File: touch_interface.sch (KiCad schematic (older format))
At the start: 15 parts

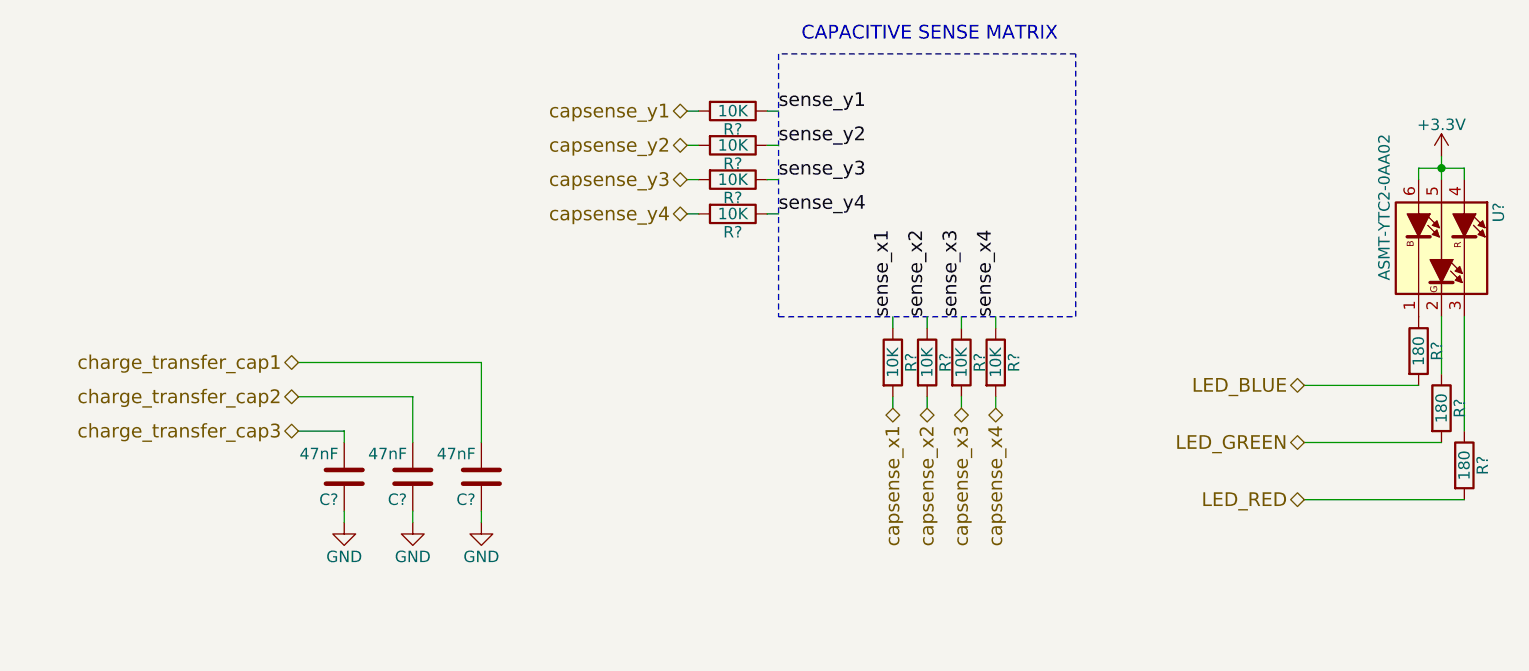
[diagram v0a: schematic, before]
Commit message: Make top-level connections between microcontroller and everything else
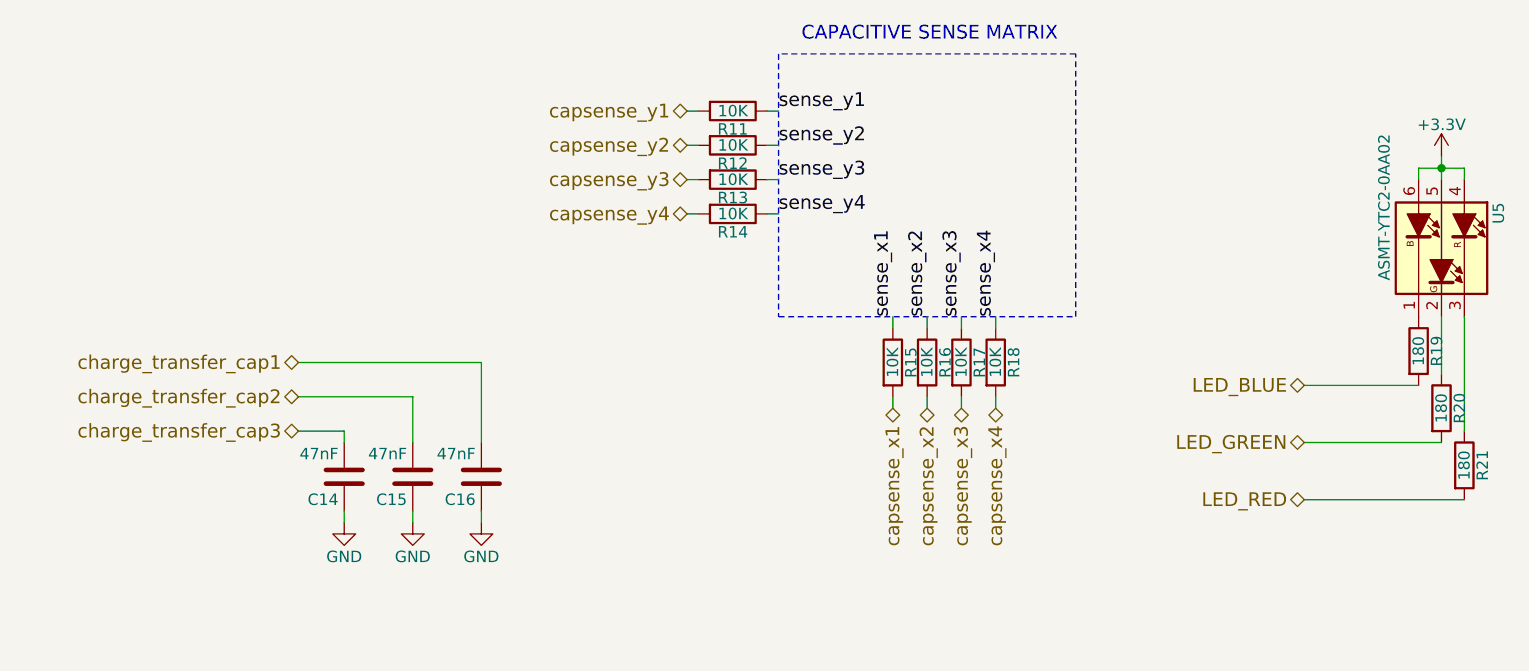
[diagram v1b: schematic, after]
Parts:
- gave numbers to parts that had none: 15
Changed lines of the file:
@@
 charge_transfer_cap3
 $Comp
-L C C?
+L C C14
 U 1 1 59A254BC
 P 2450 3950
-F 0 "C?" H 2475 4050 50  0000 L CNN
+F 0 "C14" H 2475 4050 50  0000 L CNN
 F 1 "47nF" H 2475 3850 50  0000 L CNN
 F 2 "" H 2488 3800 50  0001 C CNN
@@
 $EndComp
 $Comp
-L C C?
+L C C15
 U 1 1 59A25537
 P 2750 3950
-F 0 "C?" H 2775 4050 50  0000 L CNN
+F 0 "C15" H 2775 4050 50  0000 L CNN
 F 1 "47nF" H 2775 3850 50  0000 L CNN
 F 2 "" H 2788 3800 50  0001 C CNN
@@
 $EndComp
 $Comp
-L C C?
+L C C16
 U 1 1 59A25555
 P 3050 3950
-F 0 "C?" H 3075 4050 50  0000 L CNN
+F 0 "C16" H 3075 4050 50  0000 L CNN
 F 1 "47nF" H 3075 3850 50  0000 L CNN
 F 2 "" H 3088 3800 50  0001 C CNN
@@
 $EndComp
 $Comp
-L GND #PWR?
+L GND #PWR030
 U 1 1 59A25575
 P 2450 4150
-F 0 "#PWR?" H 2450 3900 50  0001 C CNN
+F 0 "#PWR030" H 2450 3900 50  0001 C CNN
 F 1 "GND" H 2450 4000 50  0000 C CNN
 F 2 "" H 2450 4150 50  0001 C CNN
@@
 	2450 4100 2450 4150
 $Comp
-L GND #PWR?
+L GND #PWR031
 U 1 1 59A255BB
 P 2750 4150
-F 0 "#PWR?" H 2750 3900 50  0001 C CNN
+F 0 "#PWR031" H 2750 3900 50  0001 C CNN
 F 1 "GND" H 2750 4000 50  0000 C CNN
 F 2 "" H 2750 4150 50  0001 C CNN
@@
 $EndComp
 $Comp
-L GND #PWR?
+L GND #PWR032
 U 1 1 59A255CF
 P 3050 4150
-F 0 "#PWR?" H 3050 3900 50  0001 C CNN
+F 0 "#PWR032" H 3050 3900 50  0001 C CNN
 F 1 "GND" H 3050 4000 50  0000 C CNN
 F 2 "" H 3050 4150 50  0001 C CNN
@@
 sense_x4
 $Comp
-L R R?
+L R R11
 U 1 1 59A25FAF
 P 4150 2350
-F 0 "R?" V 4230 2350 50  0000 C CNN
+F 0 "R11" V 4230 2350 50  0000 C CNN
 F 1 "10K" V 4150 2350 50  0000 C CNN
 F 2 "" V 4080 2350 50  0001 C CNN
@@
 $EndComp
 $Comp
-L R R?
+L R R12
 U 1 1 59A2606E
 P 4150 2500
-F 0 "R?" V 4230 2500 50  0000 C CNN
+F 0 "R12" V 4230 2500 50  0000 C CNN
 F 1 "10K" V 4150 2500 50  0000 C CNN
 F 2 "" V 4080 2500 50  0001 C CNN
@@
 $EndComp
 $Comp
-L R R?
+L R R13
 U 1 1 59A26093
 P 4150 2650
-F 0 "R?" V 4230 2650 50  0000 C CNN
+F 0 "R13" V 4230 2650 50  0000 C CNN
 F 1 "10K" V 4150 2650 50  0000 C CNN
 F 2 "" V 4080 2650 50  0001 C CNN
@@
 $EndComp
 $Comp
-L R R?
+L R R14
 U 1 1 59A260B9
 P 4150 2800
-F 0 "R?" V 4230 2800 50  0000 C CNN
+F 0 "R14" V 4230 2800 50  0000 C CNN
 F 1 "10K" V 4150 2800 50  0000 C CNN
 F 2 "" V 4080 2800 50  0001 C CNN
@@
 	4300 2800 4350 2800
 $Comp
-L R R?
+L R R15
 U 1 1 59A263AB
 P 4850 3450
-F 0 "R?" V 4930 3450 50  0000 C CNN
+F 0 "R15" V 4930 3450 50  0000 C CNN
 F 1 "10K" V 4850 3450 50  0000 C CNN
 F 2 "" V 4780 3450 50  0001 C CNN
@@
 $EndComp
 $Comp
-L R R?
+L R R16
 U 1 1 59A264D0
 P 5000 3450
-F 0 "R?" V 5080 3450 50  0000 C CNN
+F 0 "R16" V 5080 3450 50  0000 C CNN
 F 1 "10K" V 5000 3450 50  0000 C CNN
 F 2 "" V 4930 3450 50  0001 C CNN
@@
 $EndComp
 $Comp
-L R R?
+L R R17
 U 1 1 59A26501
 P 5150 3450
-F 0 "R?" V 5230 3450 50  0000 C CNN
+F 0 "R17" V 5230 3450 50  0000 C CNN
 F 1 "10K" V 5150 3450 50  0000 C CNN
 F 2 "" V 5080 3450 50  0001 C CNN
@@
 $EndComp
 $Comp
-L R R?
+L R R18
 U 1 1 59A26531
 P 5300 3450
-F 0 "R?" V 5380 3450 50  0000 C CNN
+F 0 "R18" V 5380 3450 50  0000 C CNN
 F 1 "10K" V 5300 3450 50  0000 C CNN
 F 2 "" V 5230 3450 50  0001 C CNN
@@
 CAPACITIVE SENSE MATRIX\n
 $Comp
-L ASMT-YTC2-0AA02 U?
+L ASMT-YTC2-0AA02 U5
 U 1 1 59A2A622
 P 7250 2950
-F 0 "U?" H 7050 3200 50  0000 L CNN
+F 0 "U5" H 7050 3200 50  0000 L CNN
 F 1 "ASMT-YTC2-0AA02" H 6750 2700 50  0000 L CNN
 F 2 "LEDs:LED_RGB_PLCC-6" H 7400 2950 50  0001 L CNN
@@
 $EndComp
 $Comp
-L +3.3V #PWR?
+L +3.3V #PWR033
 U 1 1 59A2A91F
 P 7250 2550
-F 0 "#PWR?" H 7250 2400 50  0001 C CNN
+F 0 "#PWR033" H 7250 2400 50  0001 C CNN
 F 1 "+3.3V" H 7250 2690 50  0000 C CNN
 F 2 "" H 7250 2550 50  0001 C CNN
@@
 	7350 2600 7350 2650
 $Comp
-L R R?
+L R R19
 U 1 1 59A2AF7F
 P 7150 3400
-F 0 "R?" V 7230 3400 50  0000 C CNN
+F 0 "R19" V 7230 3400 50  0000 C CNN
 F 1 "180" V 7150 3400 50  0000 C CNN
 F 2 "" V 7080 3400 50  0001 C CNN
@@
 $EndComp
 $Comp
-L R R?
+L R R20
 U 1 1 59A2AFFE
 P 7250 3650
-F 0 "R?" V 7330 3650 50  0000 C CNN
+F 0 "R20" V 7330 3650 50  0000 C CNN
 F 1 "180" V 7250 3650 50  0000 C CNN
 F 2 "" V 7180 3650 50  0001 C CNN
@@
 $EndComp
 $Comp
-L R R?
+L R R21
 U 1 1 59A2B04A
 P 7350 3900
-F 0 "R?" V 7430 3900 50  0000 C CNN
+F 0 "R21" V 7430 3900 50  0000 C CNN
 F 1 "180" V 7350 3900 50  0000 C CNN
 F 2 "" V 7280 3900 50  0001 C CNN

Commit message: Assigned some footprints and added CR1225 holder footprint
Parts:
- C14, C15, C16: footprint (none) -> Capacitors_SMD:C_0603
- R11, R12, R13, R14, R15, R16, R17, R18, R19, R20, R21: footprint (none) -> Resistors_SMD:R_0603
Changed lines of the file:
@@
 F 0 "C14" H 2475 4050 50  0000 L CNN
 F 1 "47nF" H 2475 3850 50  0000 L CNN
-F 2 "" H 2488 3800 50  0001 C CNN
+F 2 "Capacitors_SMD:C_0603" H 2488 3800 50  0001 C CNN
 F 3 "" H 2450 3950 50  0001 C CNN
 	1    2450 3950
@@
 F 0 "C15" H 2775 4050 50  0000 L CNN
 F 1 "47nF" H 2775 3850 50  0000 L CNN
-F 2 "" H 2788 3800 50  0001 C CNN
+F 2 "Capacitors_SMD:C_0603" H 2788 3800 50  0001 C CNN
 F 3 "" H 2750 3950 50  0001 C CNN
 	1    2750 3950
@@
 F 0 "C16" H 3075 4050 50  0000 L CNN
 F 1 "47nF" H 3075 3850 50  0000 L CNN
-F 2 "" H 3088 3800 50  0001 C CNN
+F 2 "Capacitors_SMD:C_0603" H 3088 3800 50  0001 C CNN
 F 3 "" H 3050 3950 50  0001 C CNN
 	1    3050 3950
@@
 F 0 "R11" V 4230 2350 50  0000 C CNN
 F 1 "10K" V 4150 2350 50  0000 C CNN
-F 2 "" V 4080 2350 50  0001 C CNN
+F 2 "Resistors_SMD:R_0603" V 4080 2350 50  0001 C CNN
 F 3 "" H 4150 2350 50  0001 C CNN
 	1    4150 2350
@@
 F 0 "R12" V 4230 2500 50  0000 C CNN
 F 1 "10K" V 4150 2500 50  0000 C CNN
-F 2 "" V 4080 2500 50  0001 C CNN
+F 2 "Resistors_SMD:R_0603" V 4080 2500 50  0001 C CNN
 F 3 "" H 4150 2500 50  0001 C CNN
 	1    4150 2500
@@
 F 0 "R13" V 4230 2650 50  0000 C CNN
 F 1 "10K" V 4150 2650 50  0000 C CNN
-F 2 "" V 4080 2650 50  0001 C CNN
+F 2 "Resistors_SMD:R_0603" V 4080 2650 50  0001 C CNN
 F 3 "" H 4150 2650 50  0001 C CNN
 	1    4150 2650
@@
 F 0 "R14" V 4230 2800 50  0000 C CNN
 F 1 "10K" V 4150 2800 50  0000 C CNN
-F 2 "" V 4080 2800 50  0001 C CNN
+F 2 "Resistors_SMD:R_0603" V 4080 2800 50  0001 C CNN
 F 3 "" H 4150 2800 50  0001 C CNN
 	1    4150 2800
@@
 F 0 "R15" V 4930 3450 50  0000 C CNN
 F 1 "10K" V 4850 3450 50  0000 C CNN
-F 2 "" V 4780 3450 50  0001 C CNN
+F 2 "Resistors_SMD:R_0603" V 4780 3450 50  0001 C CNN
 F 3 "" H 4850 3450 50  0001 C CNN
 	1    4850 3450
@@
 F 0 "R16" V 5080 3450 50  0000 C CNN
 F 1 "10K" V 5000 3450 50  0000 C CNN
-F 2 "" V 4930 3450 50  0001 C CNN
+F 2 "Resistors_SMD:R_0603" V 4930 3450 50  0001 C CNN
 F 3 "" H 5000 3450 50  0001 C CNN
 	1    5000 3450
@@
 F 0 "R17" V 5230 3450 50  0000 C CNN
 F 1 "10K" V 5150 3450 50  0000 C CNN
-F 2 "" V 5080 3450 50  0001 C CNN
+F 2 "Resistors_SMD:R_0603" V 5080 3450 50  0001 C CNN
 F 3 "" H 5150 3450 50  0001 C CNN
 	1    5150 3450
@@
 F 0 "R18" V 5380 3450 50  0000 C CNN
 F 1 "10K" V 5300 3450 50  0000 C CNN
-F 2 "" V 5230 3450 50  0001 C CNN
+F 2 "Resistors_SMD:R_0603" V 5230 3450 50  0001 C CNN
 F 3 "" H 5300 3450 50  0001 C CNN
 	1    5300 3450
@@
 F 0 "R19" V 7230 3400 50  0000 C CNN
 F 1 "180" V 7150 3400 50  0000 C CNN
-F 2 "" V 7080 3400 50  0001 C CNN
+F 2 "Resistors_SMD:R_0603" V 7080 3400 50  0001 C CNN
 F 3 "" H 7150 3400 50  0001 C CNN
 	1    7150 3400
@@
 F 0 "R20" V 7330 3650 50  0000 C CNN
 F 1 "180" V 7250 3650 50  0000 C CNN
-F 2 "" V 7180 3650 50  0001 C CNN
+F 2 "Resistors_SMD:R_0603" V 7180 3650 50  0001 C CNN
 F 3 "" H 7250 3650 50  0001 C CNN
 	1    7250 3650
@@
 F 0 "R21" V 7430 3900 50  0000 C CNN
 F 1 "180" V 7350 3900 50  0000 C CNN
-F 2 "" V 7280 3900 50  0001 C CNN
+F 2 "Resistors_SMD:R_0603" V 7280 3900 50  0001 C CNN
 F 3 "" H 7350 3900 50  0001 C CNN
 	1    7350 3900

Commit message: Create relevant BOM links, export digikey BOM
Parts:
- U5: MFR (none) -> Broadcom; MPN (none) -> ASMT-YTC2-0AA02; SPN (none) -> 516-2513-1-ND; SPR (none) -> https://www.digikey.com.au/

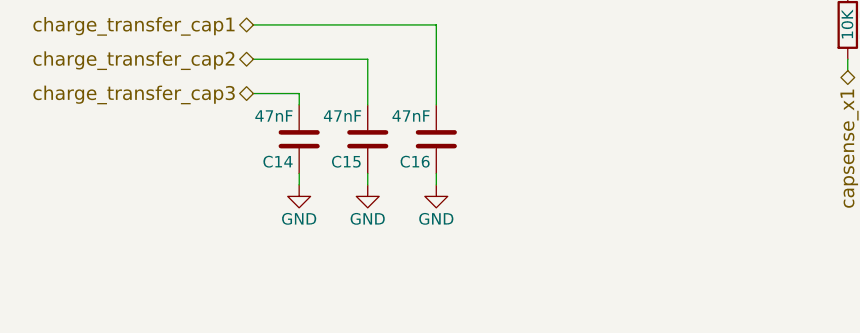
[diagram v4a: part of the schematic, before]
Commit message: Update KiCAD version, add 150uH test, add text annotating component changes
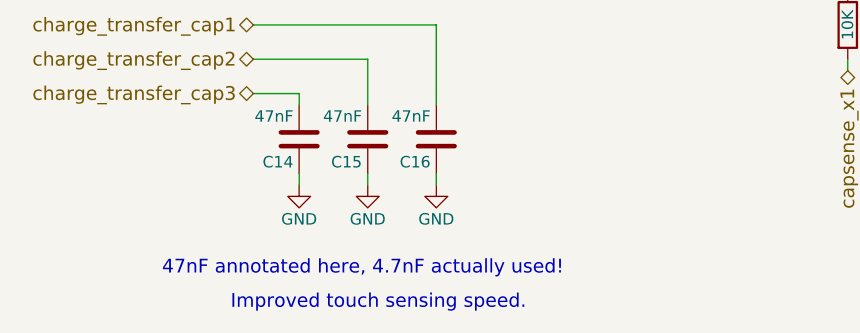
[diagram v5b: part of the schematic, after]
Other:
- note added: "47nF annotated here, 4.7nF actually used!"
- note added: "Improved touch sensing speed."
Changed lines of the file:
@@
 EESchema Schematic File Version 2
+LIBS:smart_cutlery_pcb-rescue
 LIBS:power
 LIBS:device
@@
 	7350 4050 6650 4050
 Connection ~ 7250 2600
+Text Notes 1850 4550 0    60   ~ 0
+47nF annotated here, 4.7nF actually used!
+Text Notes 2150 4700 0    60   ~ 0
+Improved touch sensing speed.
 $EndSCHEMATC
